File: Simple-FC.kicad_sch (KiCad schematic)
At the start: 55 parts, among them J1 USB_C_Receptacle_USB2.0_14P, J2 Micro_SD_Card, SW1 SW_Push, U1 RP2350A, U2 MMC5983MA, U3 LSM6DSM, U4 BMP384, U5 TPS631000, U6 W25Q128JVS, Y1 ABM8-272-T3

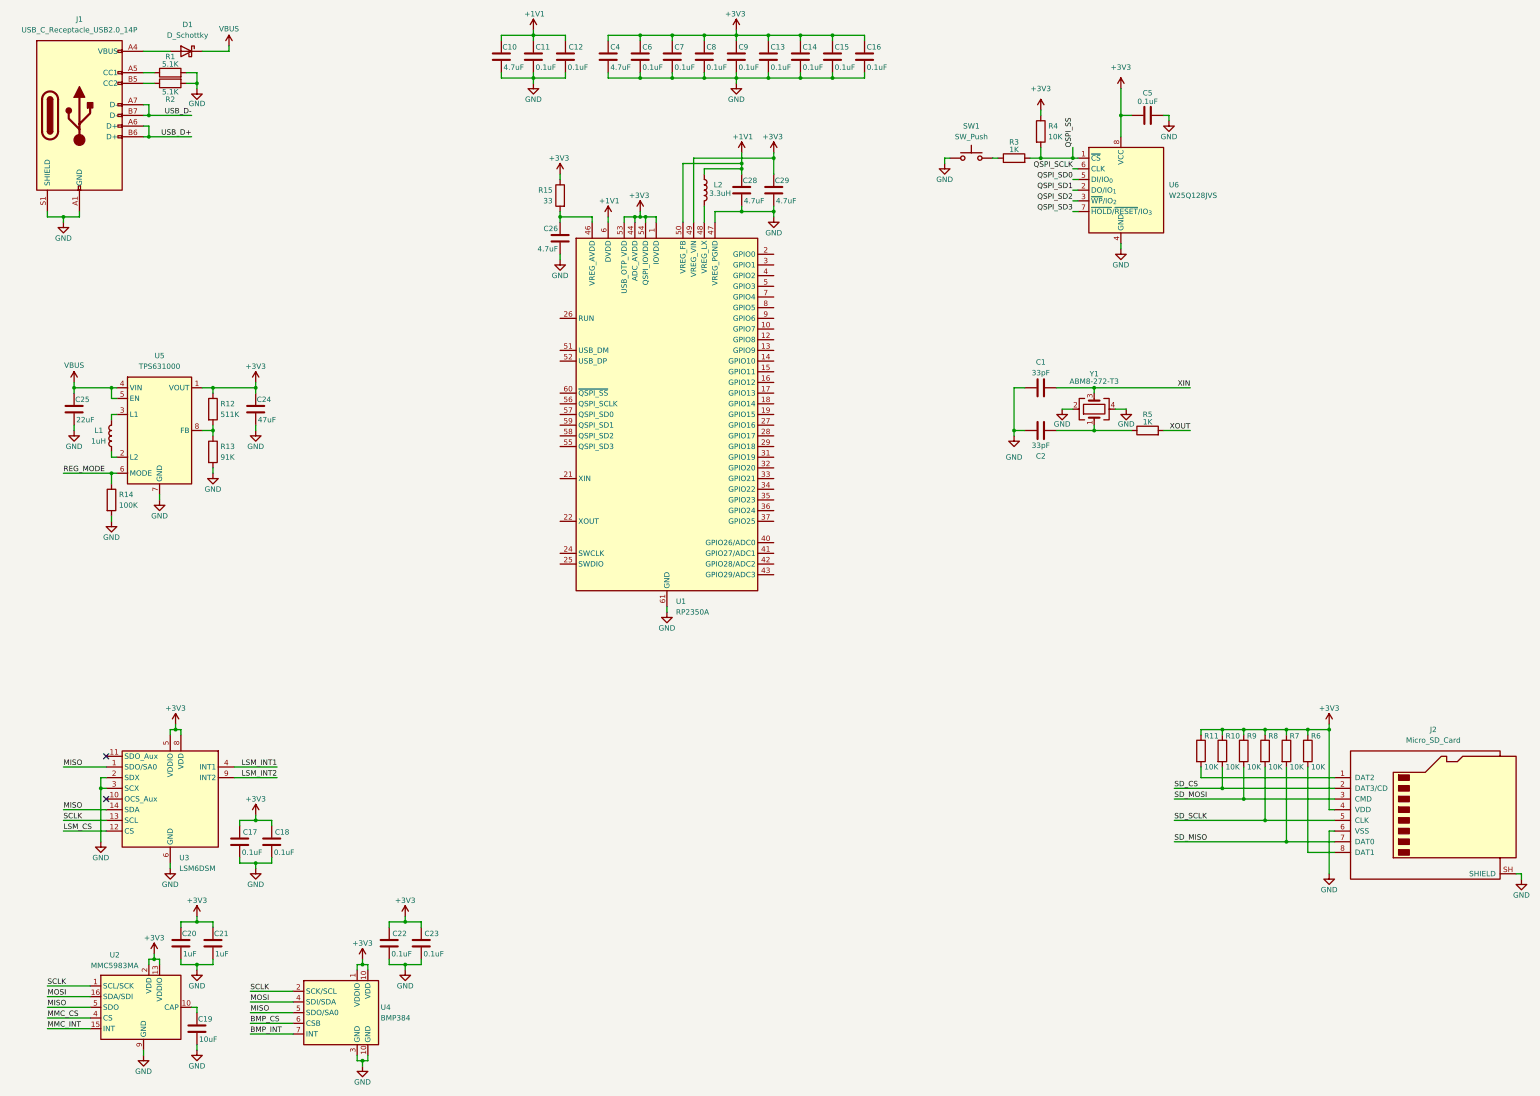
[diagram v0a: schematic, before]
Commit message: wired mcu gpio
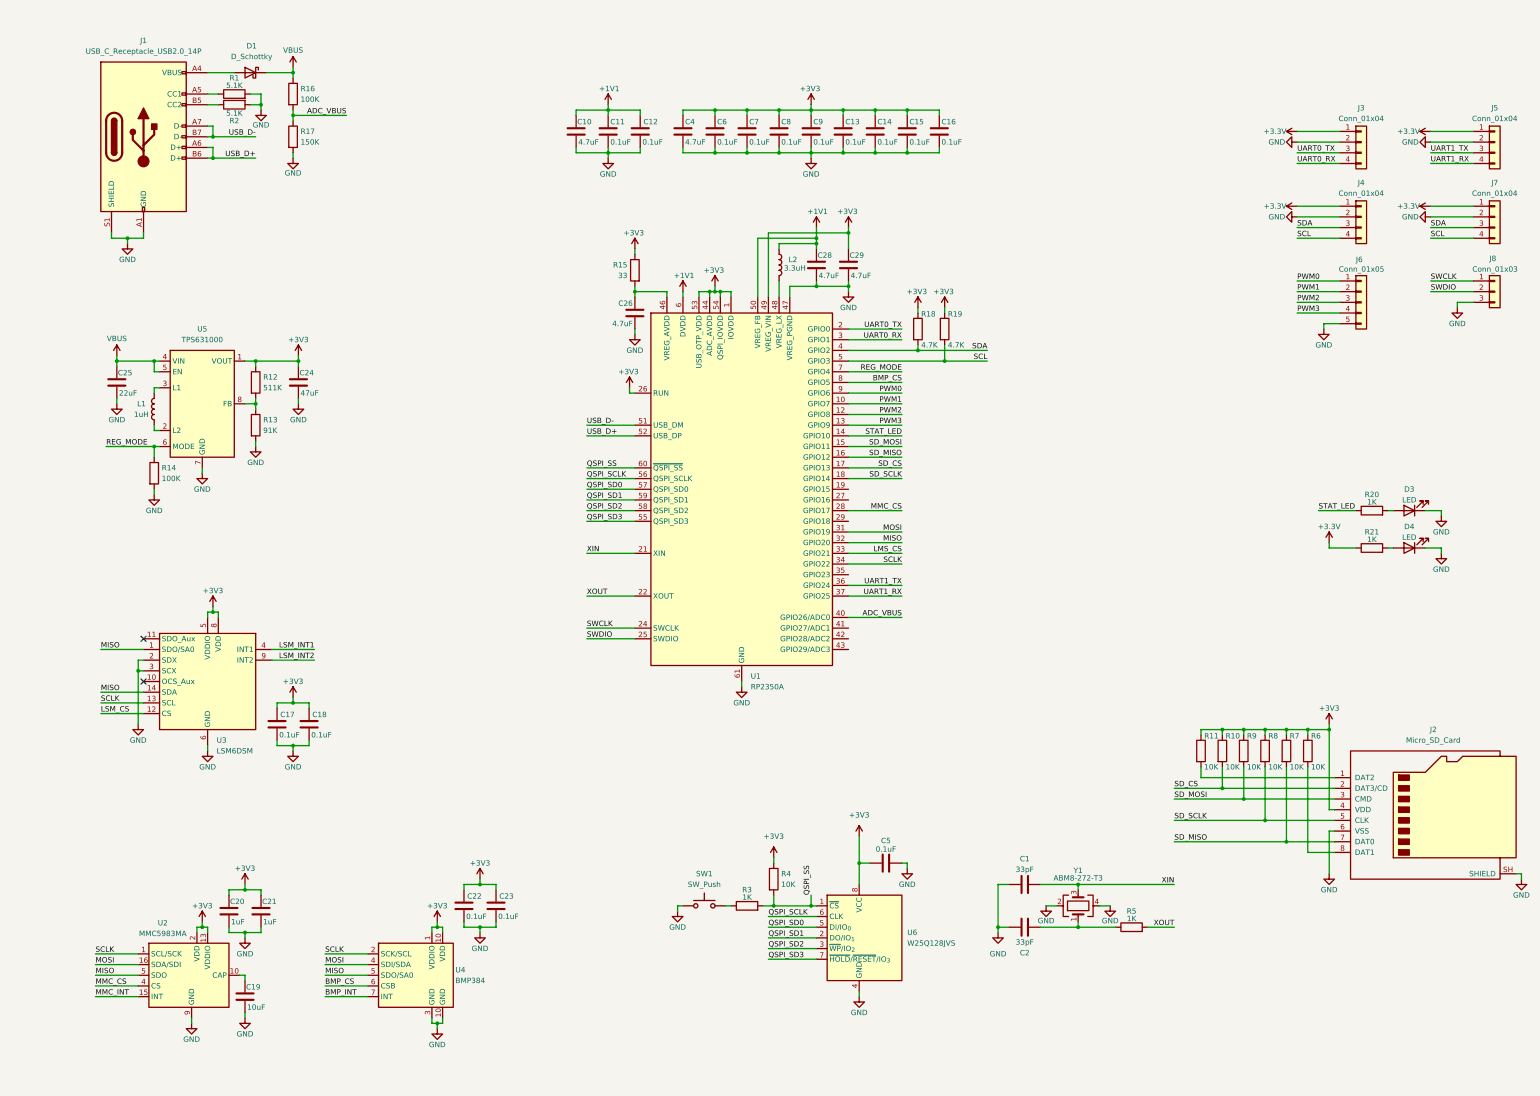
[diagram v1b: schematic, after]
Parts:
- added D3, D4: LED, LED_SMD:LED_0603_1608Metric, symbol Device:LED
- added J3, J4, J5, J7: Conn_01x04, Connector_PinHeader_2.54mm:PinHeader_1x04_P2.54mm_Vertical, symbol Connector_Generic:Conn_01x04
- added J6: Conn_01x05, symbol Connector_Generic:Conn_01x05
- added J8: Conn_01x03, Connector_JST:JST_XH_B3B-XH-A_1x03_P2.50mm_Vertical, symbol Connector_Generic:Conn_01x03
- added R16: 100K, Resistor_SMD:R_0402_1005Metric, symbol Device:R
- added R17: 150K, Resistor_SMD:R_0402_1005Metric, symbol Device:R
- added R18, R19: 4.7K, Resistor_SMD:R_0402_1005Metric, symbol Device:R
- added R20, R21: 1K, Resistor_SMD:R_0402_1005Metric, symbol Device:R
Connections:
- net +3V3: now also U1.26 (RUN), R18.1, R19.1
- net BMP_CS: now also U1.8 (GPIO5)
- net GND: now also D3.1 (K), D4.1 (K), J3.2 (Pin_2), J4.2 (Pin_2), J5.2 (Pin_2), J6.5 (Pin_5), J7.2 (Pin_2), J8.3 (Pin_3), R17.2
- net MISO: now also U1.32 (GPIO20)
- net MMC_CS: now also U1.28 (GPIO17)
- net MOSI: now also U1.31 (GPIO19)
- net QSPI_SCLK: now also U1.56 (QSPI_SCLK)
- net QSPI_SD0: now also U1.57 (QSPI_SD0)
- net QSPI_SD1: now also U1.59 (QSPI_SD1)
- net QSPI_SD2: now also U1.58 (QSPI_SD2)
- net QSPI_SD3: now also U1.55 (QSPI_SD3)
- net QSPI_SS: now also U1.60 (~{QSPI_SS})
- net REG_MODE: now also U1.7 (GPIO4)
- net SCLK: now also U1.34 (GPIO22)
- net SD_CS: now also U1.17 (GPIO13)
- net SD_MISO: now also U1.16 (GPIO12)
- net SD_MOSI: now also U1.15 (GPIO11)
- net SD_SCLK: now also U1.18 (GPIO14)
- net USB_D+: now also U1.52 (USB_DP)
- net USB_D-: now also U1.51 (USB_DM)
- net VBUS: now also R16.1
- net XIN: now also U1.21 (XIN)
- net XOUT: now also U1.22 (XOUT)
- net PWM1: now reaches U1.10 (GPIO7)
- net PWM1: now also J6.2 (Pin_2)
- net PWM2: now reaches U1.12 (GPIO8)
- net PWM2: now also J6.3 (Pin_3)
- net PWM3: now reaches U1.13 (GPIO9)
- net PWM3: now also J6.4 (Pin_4)
- net STAT_LED: now reaches U1.14 (GPIO10)
- net STAT_LED: now also R20.1
- net UART0_TX: now reaches U1.2 (GPIO0)
- net UART0_TX: now also J3.3 (Pin_3)
- net SWCLK: now reaches U1.24 (SWCLK)
- net SWCLK: now also J8.1 (Pin_1)
- net SWDIO: now reaches U1.25 (SWDIO)
- net SWDIO: now also J8.2 (Pin_2)
- net UART0_RX: now reaches U1.3 (GPIO1)
- net UART0_RX: now also J3.4 (Pin_4)
- net LMS_CS: now reaches U1.33 (GPIO21)
- net UART1_TX: now reaches U1.36 (GPIO24)
- net UART1_TX: now also J5.3 (Pin_3)
- net UART1_RX: now reaches U1.37 (GPIO25)
- net UART1_RX: now also J5.4 (Pin_4)
- net SDA: now reaches U1.4 (GPIO2)
- net SDA: now also J4.3 (Pin_3), J7.3 (Pin_3), R18.2
- net ADC_VBUS: now reaches U1.40 (GPIO26/ADC0)
- net ADC_VBUS: now also R16.2, R17.1
- net SCL: now reaches U1.5 (GPIO3)
- net SCL: now also J4.4 (Pin_4), J7.4 (Pin_4), R19.2
- net PWM0: now reaches U1.9 (GPIO6)
- net PWM0: now also J6.1 (Pin_1)
- new net: D4.2 (A), R21.2
- new net: D3.2 (A), R20.2
- new net +3.3V: J3.1 (Pin_1), J4.1 (Pin_1), J5.1 (Pin_1), J7.1 (Pin_1), R21.1
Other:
- moved on the sheet: C10, C11, C12, C13, C14, C15, C16, C17, C18, C19, C20, C21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
